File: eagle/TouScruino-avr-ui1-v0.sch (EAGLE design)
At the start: 48 parts, among them J1 AVR_ISP, Q1 8MHz, Q2 MMBT2222, Q3 8MHz, U1 ATMEGA1284P, U3 ARDUINO_SHIELD, U4 MCP73831, U5 MIC5209-3.3YS, X1 USB

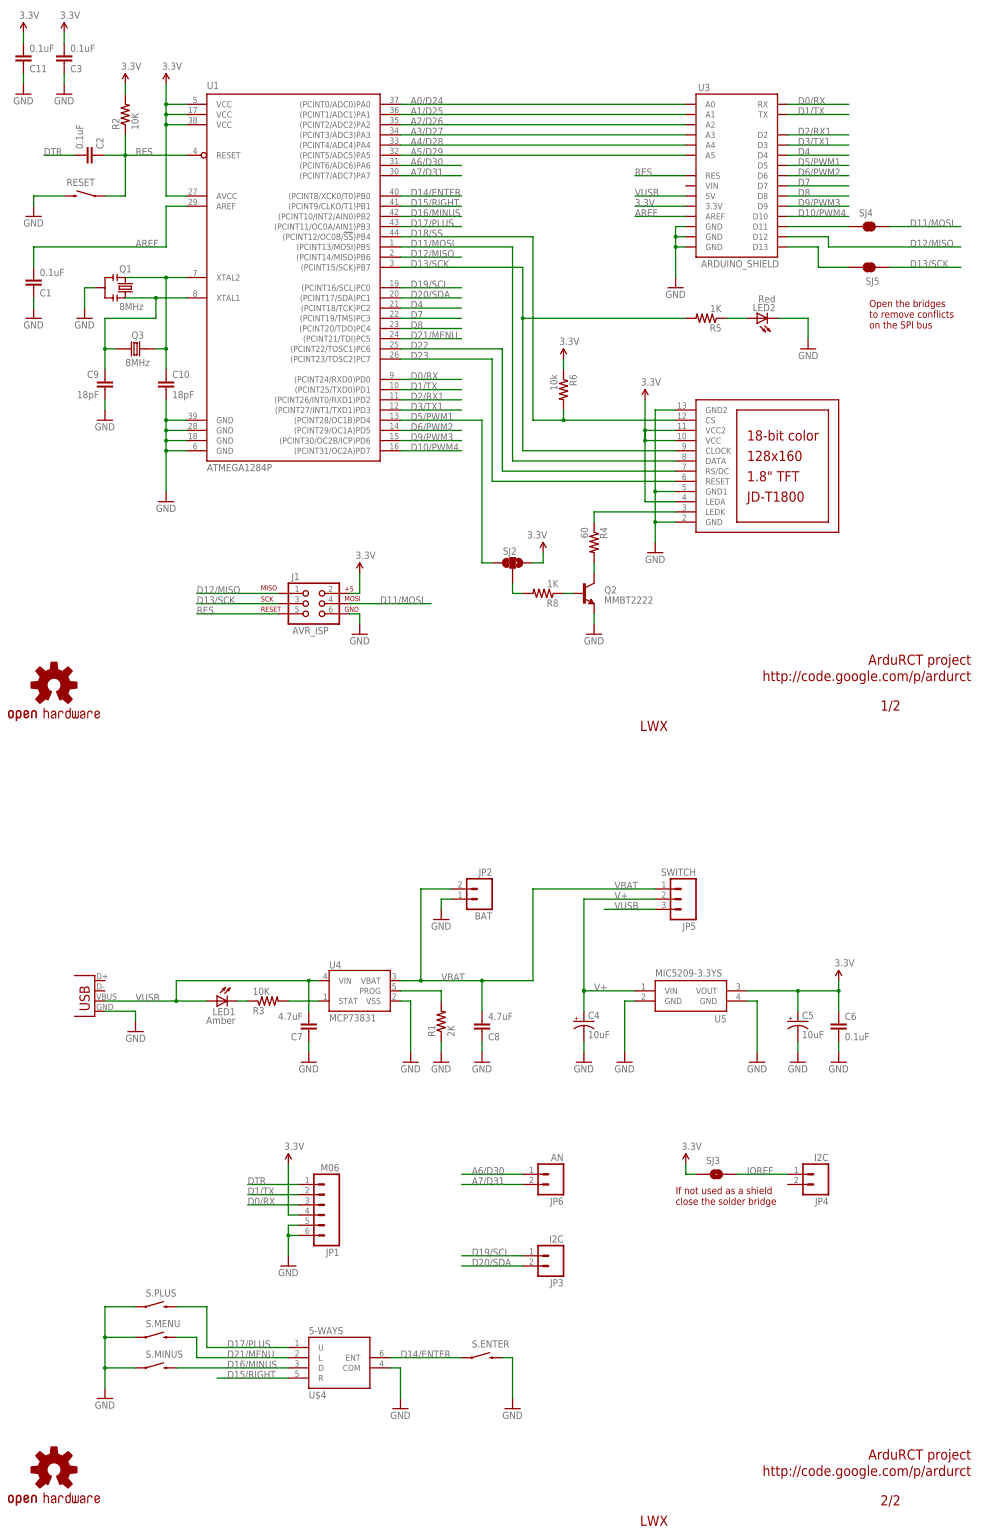
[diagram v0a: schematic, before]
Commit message: 
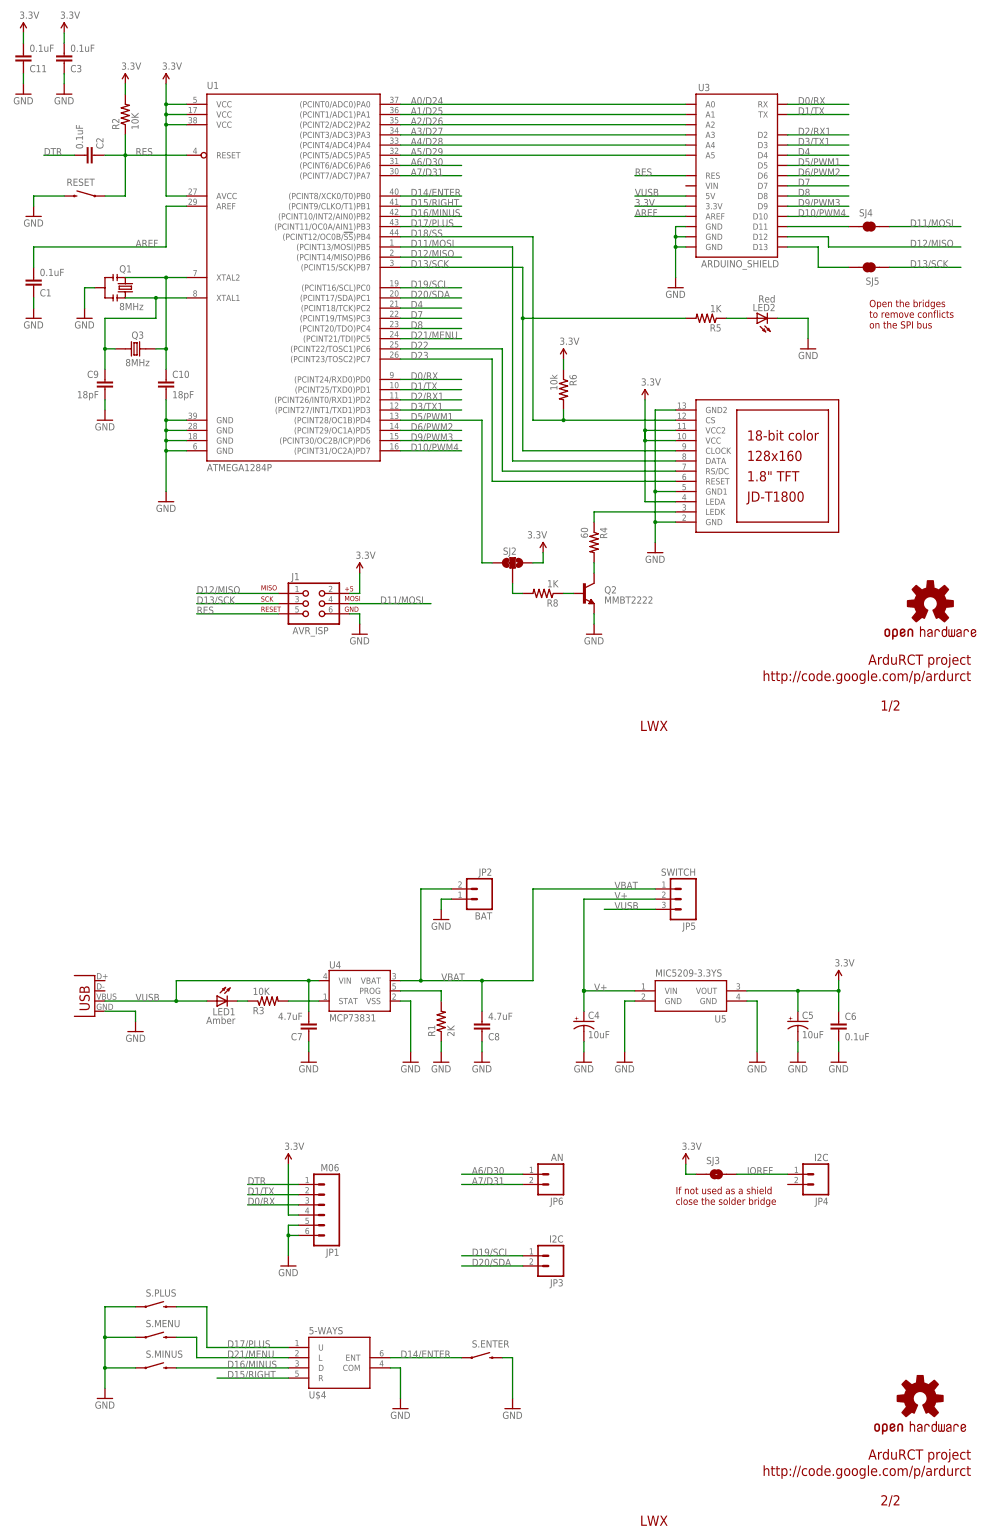
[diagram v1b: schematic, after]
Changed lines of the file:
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@@
 <instance part="X1" gate="G$1" x="25.4" y="-68.58" rot="MR0"/>
 <instance part="GND3" gate="1" x="35.56" y="-73.66" rot="MR0"/>
-<instance part="U$3" gate="G$1" x="15.24" y="12.7"/>
+<instance part="U$3" gate="G$1" x="233.68" y="33.02"/>
 <instance part="JP5" gate="G$1" x="172.72" y="-40.64" rot="R180"/>
 <instance part="P+1" gate="G$1" x="17.78" y="175.26"/>
@@
 <instance part="GND17" gate="1" x="91.44" y="25.4"/>
 <instance part="JP3" gate="G$1" x="137.16" y="-129.54" rot="R180"/>
-<instance part="U$5" gate="G$1" x="15.24" y="-182.88"/>
+<instance part="U$5" gate="G$1" x="231.14" y="-165.1"/>
 <instance part="JP4" gate="G$1" x="203.2" y="-109.22" rot="R180"/>
 <instance part="SJ3" gate="1" x="180.34" y="-109.22"/>

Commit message: 
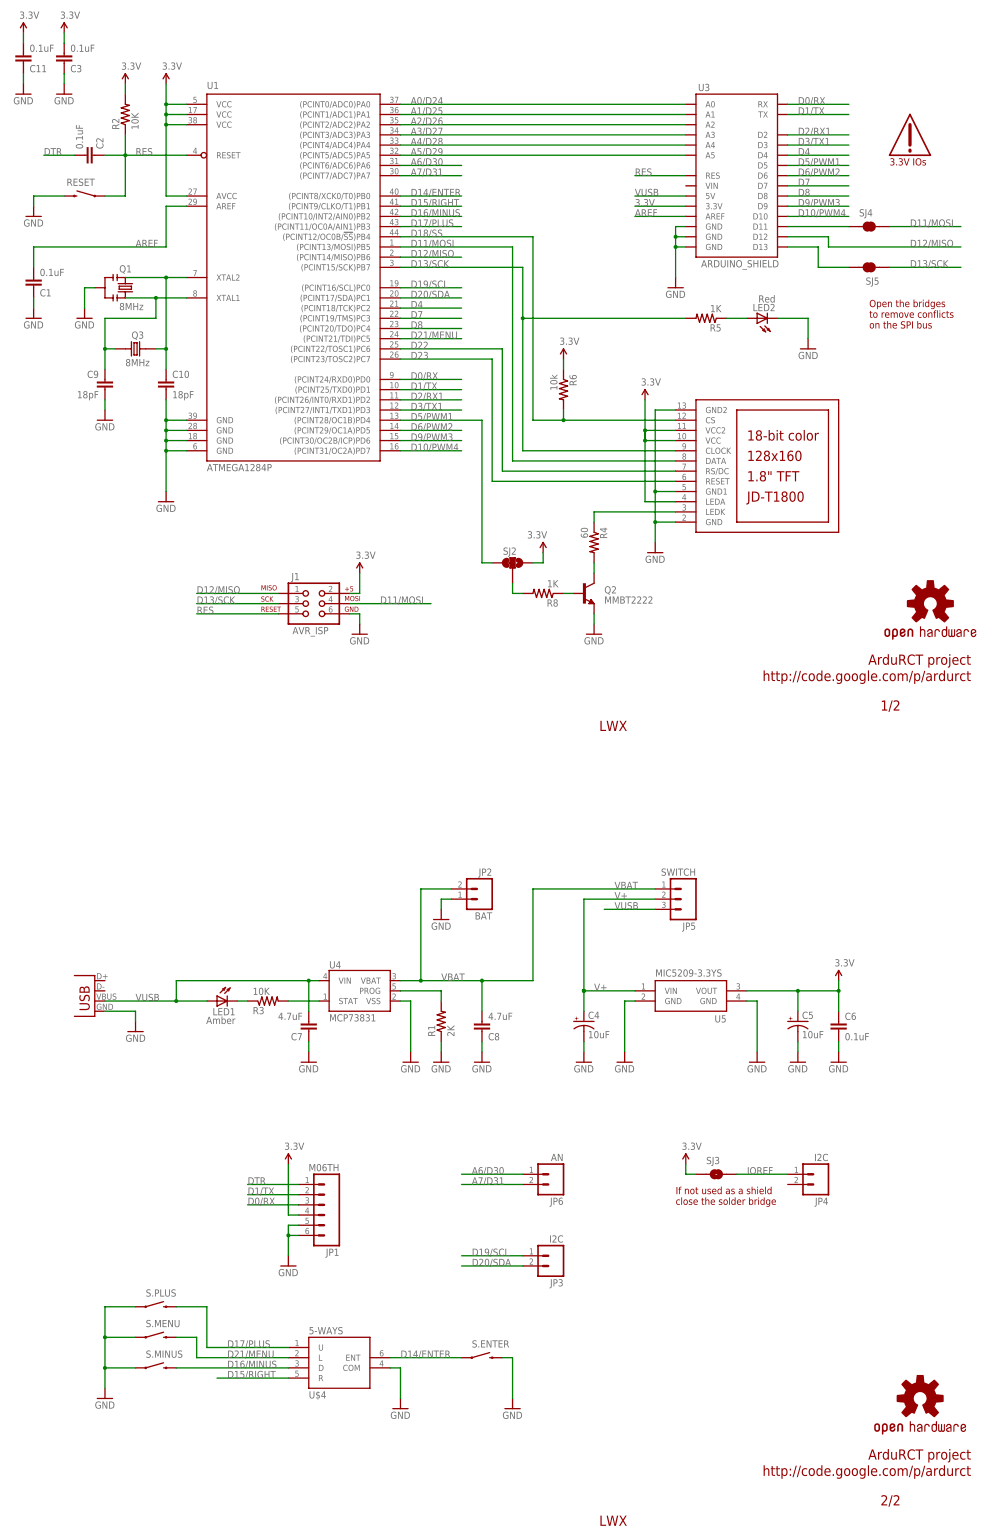
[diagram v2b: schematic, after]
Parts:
- added U$6: 3.3V_IO, wibauxl:3.3V_IO
- JP1: value M06 -> M06TH; device wibauxl:M06 -> wibauxl:M06TH
- JP5: device wibauxl:M03 -> wibauxl:M03LP
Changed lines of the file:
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@@
 <part name="GND3" library="SparkFun" deviceset="GND" device=""/>
 <part name="U$3" library="SparkFun" deviceset="OSHW-LOGO" device="M"/>
-<part name="JP5" library="wibauxl" deviceset="M03" device="" value="SWITCH"/>
+<part name="JP5" library="wibauxl" deviceset="M03" device="LP" value="SWITCH"/>
 <part name="P+1" library="SparkFun" deviceset="3.3V" device=""/>
 <part name="P+2" library="SparkFun" deviceset="3.3V" device=""/>
 <part name="P+3" library="SparkFun" deviceset="3.3V" device=""/>
 <part name="GND16" library="SparkFun" deviceset="GND" device=""/>
-<part name="JP1" library="wibauxl" deviceset="M06" device=""/>
+<part name="JP1" library="wibauxl" deviceset="M06" device="TH"/>
 <part name="GND14" library="SparkFun" deviceset="GND" device=""/>
 <part name="P+8" library="SparkFun" deviceset="3.3V" device=""/>
@@
 <part name="SJ4" library="SparkFun" deviceset="SOLDERJUMPER" device="TRACE" value=""/>
 <part name="SJ5" library="SparkFun" deviceset="SOLDERJUMPER" device="TRACE" value=""/>
+<part name="U$6" library="wibauxl" deviceset="3.3V_IO" device=""/>
 </parts>
 <sheets>
 <sheet>
 <plain>
-<text x="161.29" y="1.27" size="2.54" layer="94" font="vector">LWX</text>
+<text x="151.13" y="1.27" size="2.54" layer="94" font="vector">LWX</text>
 <text x="221.234" y="6.35" size="2.54" layer="94" font="vector">1/2</text>
-<text x="161.29" y="-196.85" size="2.54" layer="94" font="vector">LWX</text>
+<text x="151.13" y="-196.85" size="2.54" layer="94" font="vector">LWX</text>
 <text x="221.234" y="-191.77" size="2.54" layer="94" font="vector">2/2</text>
 <text x="170.18" y="-116.84" size="1.778" layer="94">If not used as a shield
@@
 <instance part="SJ4" gate="1" x="218.44" y="127"/>
 <instance part="SJ5" gate="1" x="218.44" y="116.84" rot="R180"/>
+<instance part="U$6" gate="G$1" x="228.6" y="147.32"/>
 </instances>
 <busses>
